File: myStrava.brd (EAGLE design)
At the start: 64.8 x 45.4 mm, 53 parts, among them Y1 16MHz

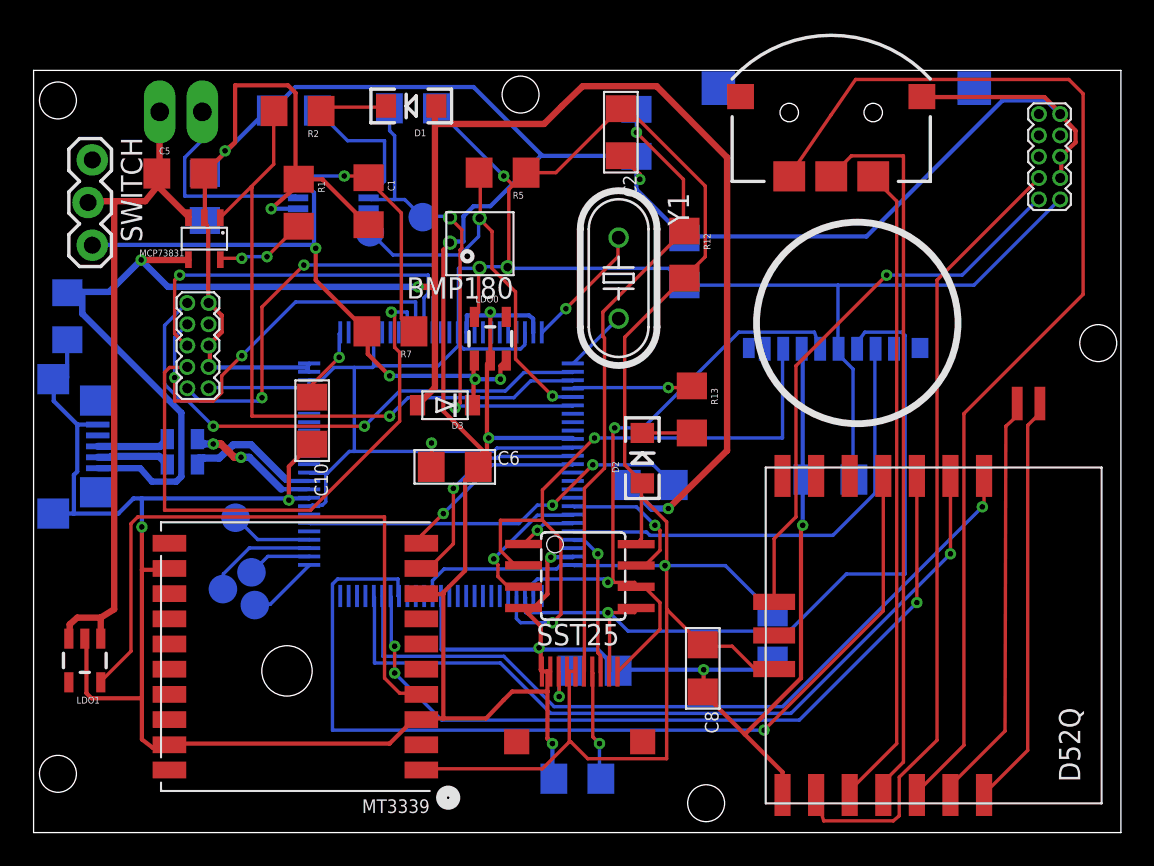
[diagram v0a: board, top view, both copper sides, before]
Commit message: Recablage du D52 pour simplifier
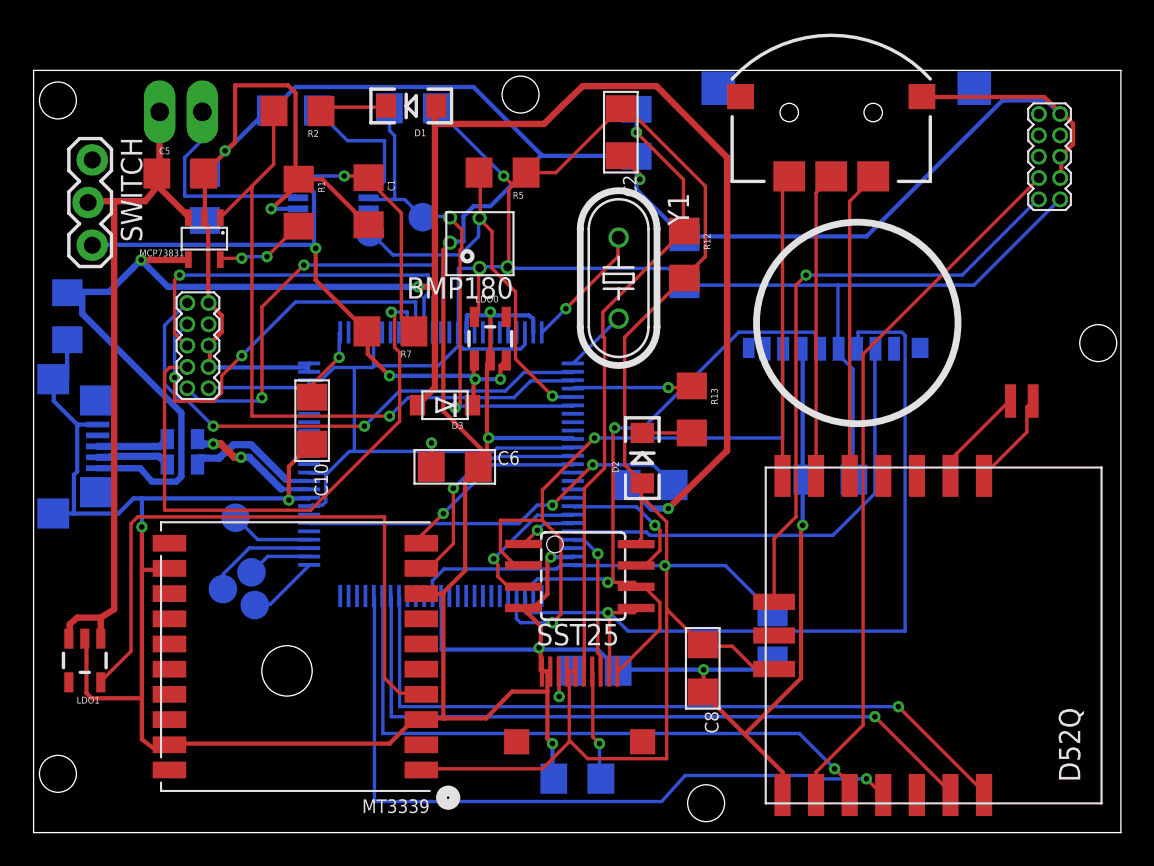
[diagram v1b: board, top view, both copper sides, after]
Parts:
- moved SPK 3.03 mm to (57.9, 24.7), turned to 0 degrees
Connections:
- removed net N$11 (its old number): N550.P006, NAV.2
- new net N$3: N550.P017, SPK.P$2
- net MK_RX3: now also N550.P006; no longer N550.P017
- net MK_TX3: now also N550.P007; no longer N550.P016
- net N$10: now also N550.P013, NAV.2; no longer N550.P007, NAV.T
- net N$18: now also N550.P008; no longer N550.P015
- net N$21: now also N550.P011; no longer N550.P014
- net N$7: now also N550.P016, SPK.P$1; no longer N550.P002, NAV.1
- net N$8: now also N550.P012, NAV.1; no longer N550.P011, SPK.P$1
- net N$9: now also N550.P031, NAV.T; no longer N550.P008, SPK.P$2
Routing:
- net N$7: track 66.8 -> 5.98 mm
- net N$11 (its old number): track 38.6 -> 0.00 mm
- net N$10: track 43.4 -> 18.4 mm
- net N$21: track 57.6 -> 43.7 mm
- net MK_RX3: track 47.4 -> 37.9 mm
- net N$8: track 24.7 -> 18.0 mm
- net N$9: track 24.9 -> 18.2 mm
- net N$3: track 0.00 -> 5.69 mm
- net N$12: track 47.7 -> 42.2 mm
- net N$18: track 47.5 -> 42.5 mm, vias 3 -> 1
- net MK_TX3: track 48.1 -> 43.8 mm
- net N$11: track 33.2 -> 36.0 mm
- net MK_DO: track 48.7 -> 51.0 mm

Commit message: Envoi a OSH park
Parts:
- removed BMP180: BMP180, SparkFun-Sensors:BMP180
- added MS5637: MS5637, MS5637:MS5637
- MT3333: value GTK -> TITAN2
- moved SHARP 1.60 mm to (34.6, 3.87)
- renumbered MT3339 to MT3333, N550 to D52Q
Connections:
- net GND: now also MS5637.GND; no longer BMP180.GND_
- net MK_SCL: now also MS5637.SCL; no longer BMP180.SCL_
- net MK_SDA: now also MS5637.SDA; no longer BMP180.SDA_
- net VCC: now also MS5637.VDD; no longer BMP180.VDD, BMP180.VDDIO
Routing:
- net VCC: track 225.4 -> 235.3 mm
- net GND: track 338.5 -> 330.7 mm
- net MK_SCL: track 26.4 -> 31.9 mm, vias 1 -> 3
- net MK_SDA: track 29.8 -> 26.4 mm, vias 1 -> 2
- net N$27: track 37.3 -> 38.8 mm
- net MK_SCLK: track 39.0 -> 40.6 mm
- net MK_DO: track 51.0 -> 52.6 mm
- net N$26: track 6.58 -> 5.02 mm
- net N$22: track 8.99 -> 10.5 mm

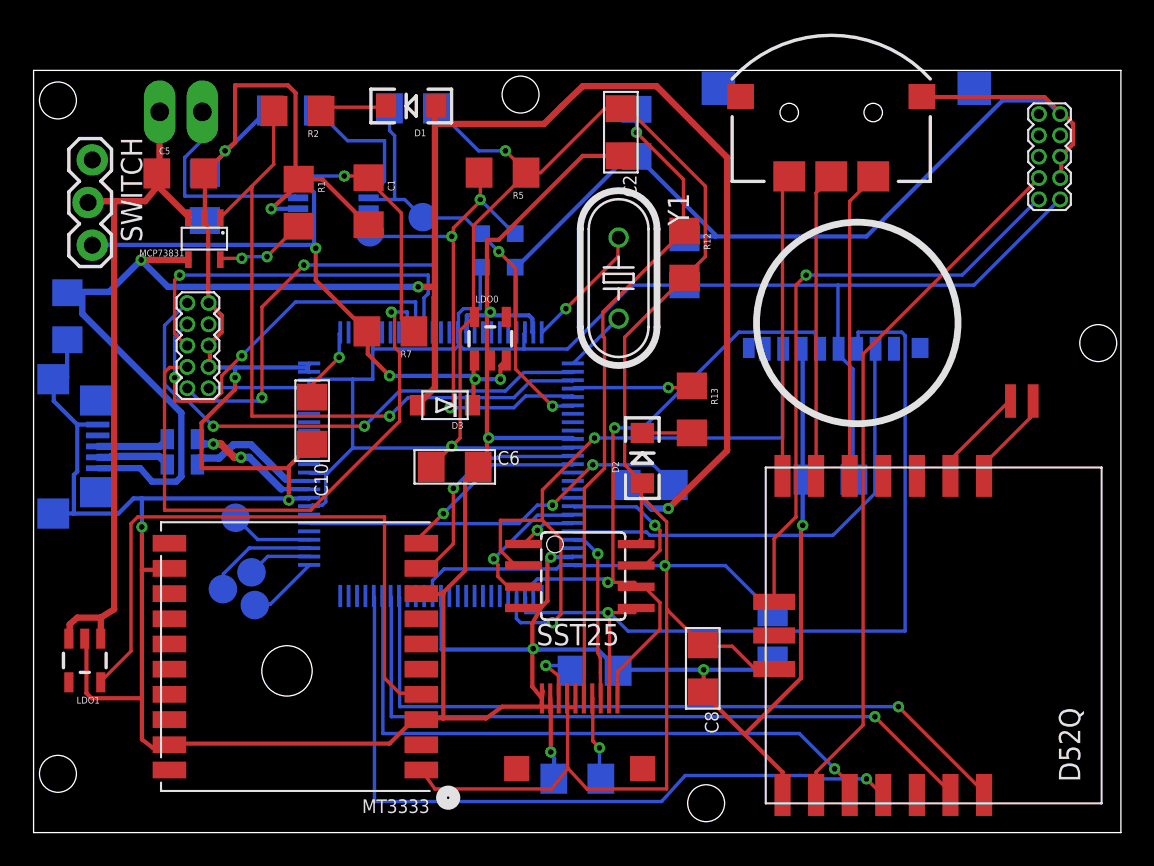
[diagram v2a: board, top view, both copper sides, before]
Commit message: Ajout du M8 en face inferieure
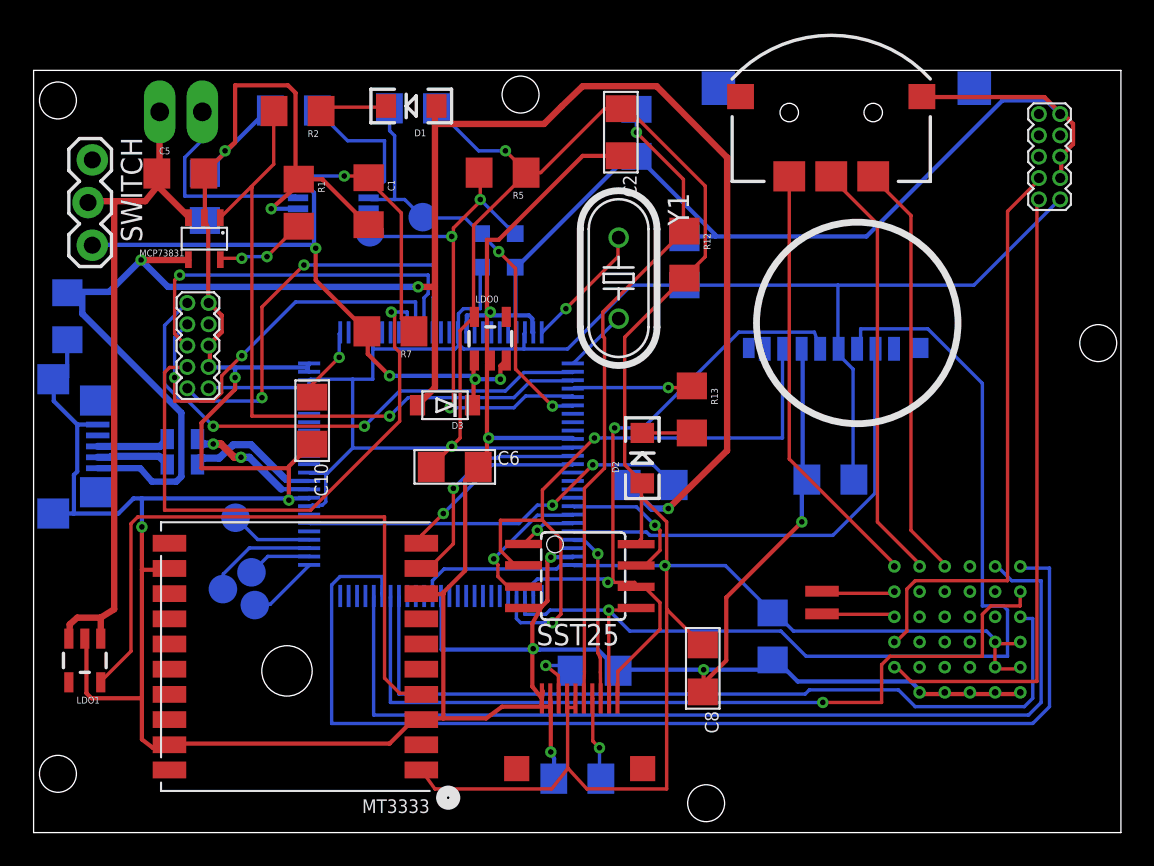
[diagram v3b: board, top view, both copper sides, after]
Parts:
- D52Q: value ANTAP28 -> N548; device D52Q:ANTAP -> N548:N548
- moved SPK 15.6 mm to (48.0, 12.7), turned to 90 degrees
- moved D52Q 14.9 mm to (58.8, 15.8), turned to 180 degrees
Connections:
- removed net MK_RX3: D52Q.P006, MK20DN512.95
- removed net MK_TX3: D52Q.P007, MK20DN512.96
- new net N$13: D52Q.P024, MK20DN512.93
- new net N$29: D52Q.P002, MK20DN512.96
- net GND: now also D52Q.A2, D52Q.A3, D52Q.A4, D52Q.A5, D52Q.A6; no longer D52Q.GND
- net N$10: now also D52Q.P003; no longer D52Q.P013
- net N$12: now also D52Q.SWDCLK; no longer D52Q.SWDCLCK
- net N$18: now also D52Q.P030; no longer D52Q.P008
- net N$21: now also D52Q.P031, MK20DN512.95; no longer D52Q.P011, MK20DN512.93
- net N$3: now also D52Q.P012, SPK.P$1; no longer D52Q.P017, SPK.P$2
- net N$7: now also D52Q.P009, SPK.P$2; no longer D52Q.P016, SPK.P$1
- net N$8: now also D52Q.P008; no longer D52Q.P012
- net N$9: now also D52Q.P005; no longer D52Q.P031
- net VCC: now also D52Q.B5, D52Q.B6, D52Q.C5, D52Q.C6; no longer D52Q.VCC
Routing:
- net N$29: track 0.00 -> 57.5 mm
- net N$13: track 0.00 -> 49.8 mm
- net MK_TX3: track 43.8 -> 0.00 mm, vias 1 -> 0
- net MK_RX3: track 37.9 -> 0.00 mm, vias 1 -> 0
- net N$21: track 43.7 -> 65.8 mm, vias 1 -> 0
- net VCC: track 235.3 -> 249.2 mm
- net MK_DO: track 52.6 -> 65.5 mm
- net N$8: track 18.0 -> 25.8 mm
- net N$12: track 42.2 -> 34.4 mm
- net N$18: track 42.5 -> 49.9 mm
- net N$9: track 18.2 -> 25.4 mm
- net N$10: track 18.4 -> 25.0 mm
- net GND: track 330.7 -> 337.2 mm
- net N$11: track 36.0 -> 37.6 mm, vias 1 -> 0
- net N$7: track 5.98 -> 4.49 mm
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
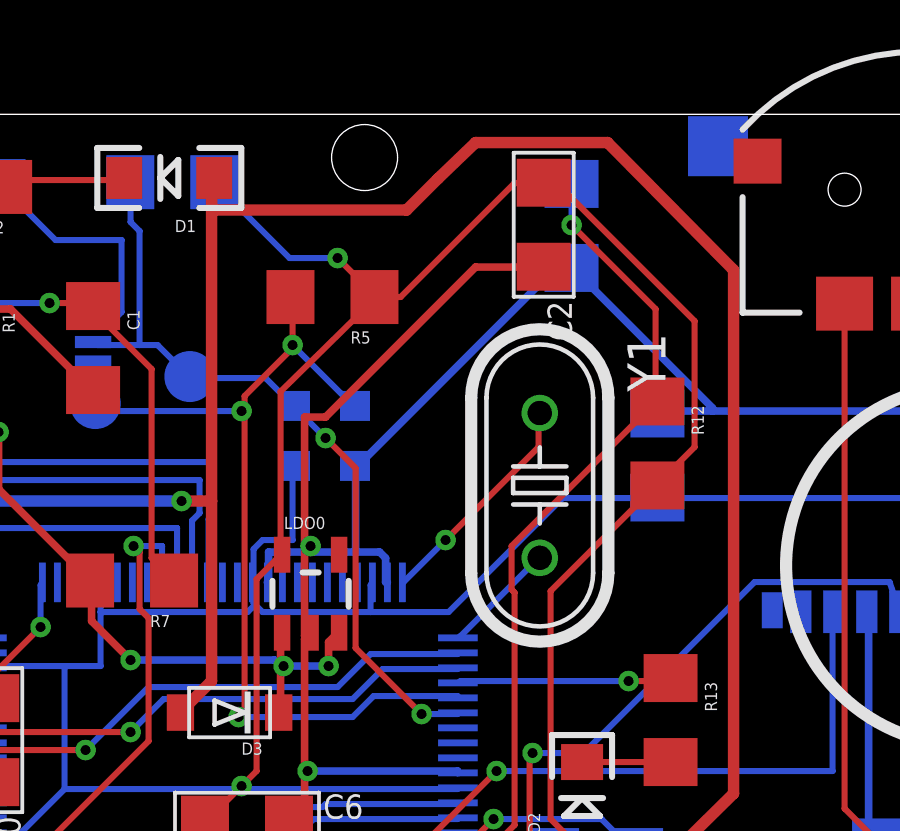
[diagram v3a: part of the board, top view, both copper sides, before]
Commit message: Modif d'une via
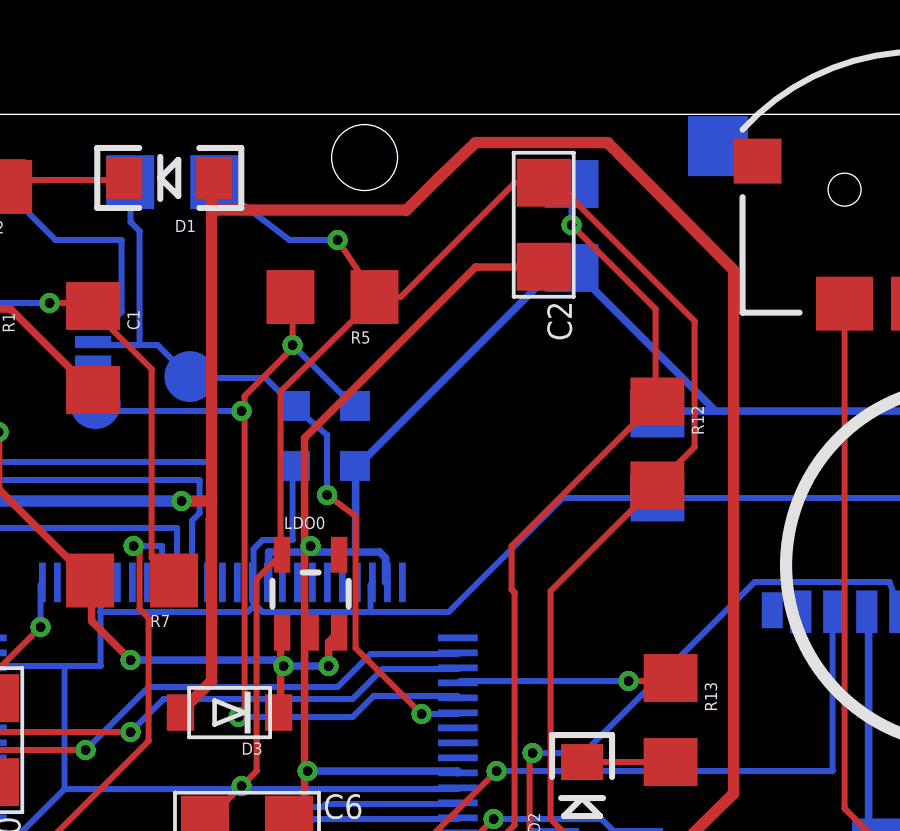
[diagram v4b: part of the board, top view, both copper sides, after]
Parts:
- removed Y1: 16MHz, SparkFun-FreqCtrl:HC49U-V
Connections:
- removed net N$14: MK20DN512.51, Y1.2
- removed net N$19: MK20DN512.50, Y1.1
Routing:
- net N$19: track 7.56 -> 0.00 mm, vias 1 -> 0
- net N$14: track 3.83 -> 0.00 mm
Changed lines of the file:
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@@
 <element name="R8" library="SparkFun-Resistors" package="0805" value="33ohm" x="8.86" y="23.43" rot="MR180"/>
 <element name="R9" library="SparkFun-Resistors" package="0805" value="33ohm" x="8.86" y="21.92" rot="MR180"/>
-<element name="Y1" library="SparkFun-FreqCtrl" package="HC49U-V" value="16MHz" x="34.84" y="33.02" smashed="yes" rot="R270">
-<attribute name="NAME" x="37.761" y="38.1" size="1.27" layer="25" ratio="10" rot="R270"/>
-<attribute name="VALUE" x="30.649" y="38.1" size="1.27" layer="27" ratio="10" rot="R270"/>
-</element>
 <element name="C9" library="microbuilder" package="1206" value="0.1uF" x="38.76" y="34.02" rot="MR90"/>
 <element name="C10" library="microbuilder" package="1206" value="0.1uF" x="16.59" y="24.53" rot="R270"/>
@@
 <wire x1="35.8" y1="40.2" x2="35.9" y2="40.27" width="0.254" layer="16"/>
 <wire x1="32.7" y1="40.3" x2="34.9" y2="40.3" width="0.254" layer="1"/>
-<wire x1="27.7" y1="35.3" x2="32.7" y2="40.3" width="0.254" layer="1"/>
-<wire x1="27" y1="35.3" x2="27.7" y2="35.3" width="0.254" layer="1"/>
+<wire x1="27" y1="34.6" x2="32.7" y2="40.3" width="0.254" layer="1"/>
 <wire x1="27" y1="28" x2="27" y2="31" width="0.254" layer="1"/>
-<wire x1="27" y1="31" x2="27" y2="35.3" width="0.254" layer="1"/>
+<wire x1="27" y1="31" x2="27" y2="34.6" width="0.254" layer="1"/>
 <wire x1="34.9" y1="40.3" x2="34.97" y2="40.31" width="0.254" layer="1"/>
 <wire x1="27" y1="28" x2="27.2" y2="28.1099" width="0.254" layer="1"/>
@@
 <wire x1="30.9" y1="25.4" x2="32.1" y2="25.4" width="0.2032" layer="16"/>
 <wire x1="28.7" y1="27.6" x2="30.9" y2="25.4" width="0.2032" layer="1"/>
-<wire x1="28.7" y1="33.6" x2="28.7" y2="27.6" width="0.2032" layer="1"/>
-<wire x1="27.7" y1="34.6" x2="28.7" y2="33.6" width="0.2032" layer="1"/>
-<wire x1="26.7" y1="35.6" x2="27.7" y2="34.6" width="0.2032" layer="16"/>
+<wire x1="28.7" y1="32" x2="28.7" y2="27.6" width="0.2032" layer="1"/>
+<wire x1="27.75" y1="32.7" x2="28.7" y2="32" width="0.2032" layer="1"/>
+<wire x1="27.75" y1="32.7" x2="27.75" y2="34.7" width="0.2032" layer="16"/>
+<wire x1="27.75" y1="34.7" x2="26.7" y2="35.6" width="0.2032" layer="16"/>
 <wire x1="32.1" y1="25.4" x2="32.11" y2="25.439990625" width="0.2032" layer="16"/>
 <wire x1="26.7" y1="35.6" x2="26.68" y2="35.67" width="0.2032" layer="16"/>
 <via x="30.9" y="25.4" extent="1-16" drill="0.3302"/>
-<via x="27.7" y="34.6" extent="1-16" drill="0.3302"/>
+<via x="27.75" y="32.7" extent="1-16" drill="0.3302"/>
 </signal>
 <signal name="MK_SCL">
@@
 <wire x1="4.8" y1="13.3" x2="4" y2="12.8" width="0.381" layer="1"/>
 <wire x1="4.8" y1="37.6" x2="4.8" y2="13.3" width="0.381" layer="1"/>
-</signal>
-<signal name="N$14">
-<contactref element="Y1" pad="2"/>
-<contactref element="MK20DN512" pad="51"/>
-<wire x1="34.8" y1="30.6" x2="32.2" y2="28" width="0.2032" layer="16"/>
-<wire x1="32.2" y1="28" x2="32.11" y2="27.939990625" width="0.2032" layer="16"/>
-<wire x1="34.8" y1="30.6" x2="34.84" y2="30.607" width="0.2032" layer="16"/>
-</signal>
-<signal name="N$19">
-<contactref element="MK20DN512" pad="50"/>
-<contactref element="Y1" pad="1"/>
-<wire x1="31.7" y1="31.2" x2="30.3" y2="29.8" width="0.2032" layer="16"/>
-<wire x1="34.8" y1="34.3" x2="31.7" y2="31.2" width="0.2032" layer="1"/>
-<wire x1="34.8" y1="35.4" x2="34.8" y2="34.3" width="0.2032" layer="1"/>
-<wire x1="30.3" y1="29.8" x2="30.259990625" y2="29.79" width="0.2032" layer="16"/>
-<wire x1="34.8" y1="35.4" x2="34.84" y2="35.433" width="0.2032" layer="1"/>
-<via x="31.7" y="31.2" extent="1-16" drill="0.3302"/>
 </signal>
 <signal name="N$23">
@@
 <wire x1="37.7" y1="13.2" x2="37.75" y2="13.25" width="0.2032" layer="1"/>
 <via x="37.6" y="15.9" extent="1-16" drill="0.3302"/>
-<wire x1="26.5" y1="40.6" x2="24" y2="43.1" width="0.2032" layer="16"/>
-<wire x1="28.1" y1="40.6" x2="26.5" y2="40.6" width="0.2032" layer="16"/>
-<wire x1="29.3" y1="39.4" x2="28.1" y2="40.6" width="0.2032" layer="1"/>
+<wire x1="26.5" y1="41.2" x2="24" y2="43.1" width="0.2032" layer="16"/>
+<wire x1="28.1" y1="41.2" x2="26.5" y2="41.2" width="0.2032" layer="16"/>
+<wire x1="29.3" y1="39.4" x2="28.1" y2="41.2" width="0.2032" layer="1"/>
 <wire x1="24" y1="43.1" x2="23.99" y2="43.13" width="0.2032" layer="16"/>
 <wire x1="29.3" y1="39.4" x2="29.33" y2="39.3" width="0.2032" layer="1"/>
-<via x="28.1" y="40.6" extent="1-16" drill="0.3302"/>
+<via x="28.1" y="41.2" extent="1-16" drill="0.3302"/>
 <wire x1="26.2" y1="31.1" x2="26.3" y2="30.8" width="0.2032" layer="1"/>
 <wire x1="26.2" y1="36.15" x2="26.2" y2="31.1" width="0.2032" layer="1"/>
